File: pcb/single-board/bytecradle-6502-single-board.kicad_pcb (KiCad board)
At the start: 2 copper layers, 224.9 x 116.2 mm, 88 parts, among them J1 USB_B, J2 EXPBUS1, J3 EXPBUS2, J4 VIA, J5 UART1, J6 UART2, J7 Serial, J8 Serial, SW1 SW_SPDT, SW2 RESET, SW3 NMI, U1 74HC14, U10 74HC273, U11 74HC273, U12 74HC245, U13 74HC245, U14 74HC10, U15 SST39SF040, U16 AS6C4008, U17 CY62256, U18 74HC688, U19 W65C22NxP, U2 W65C02, U20 74HC688, U21 W65C51NxP, U22 74HC688, U23 W65C51NxP, U3 74HC688, U4 74HC08, U5 74HC688, U6 74HC688, U7 74HC04, U8 74HC10, U9 74HC00, X1 32MHz, Y1 1.8432 MHz, Y2 1.8432 MHz

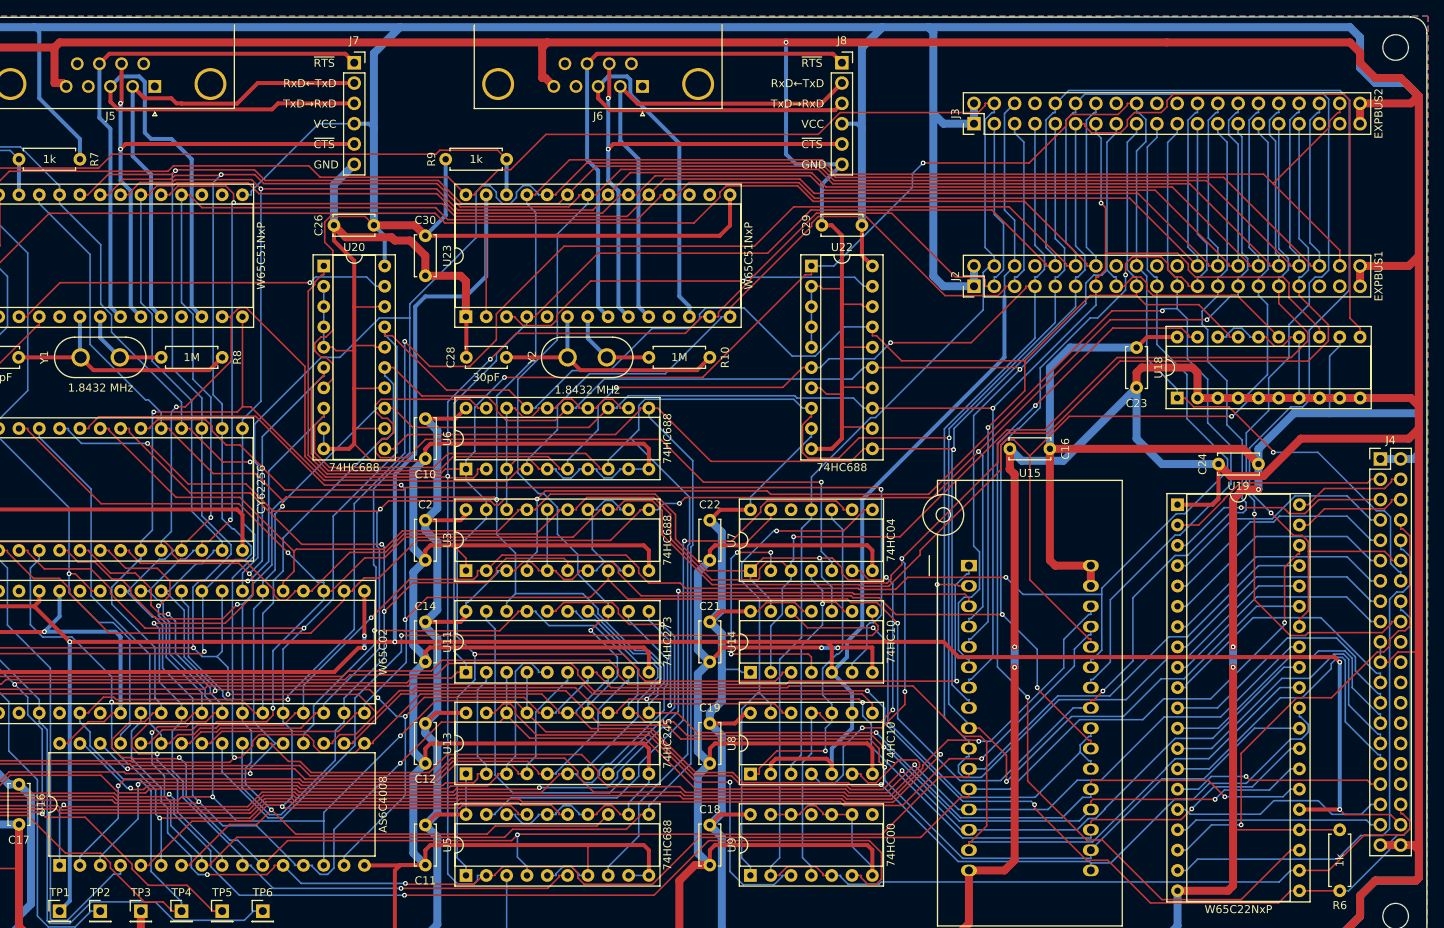
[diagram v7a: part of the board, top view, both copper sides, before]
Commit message: Revising board and adding logo
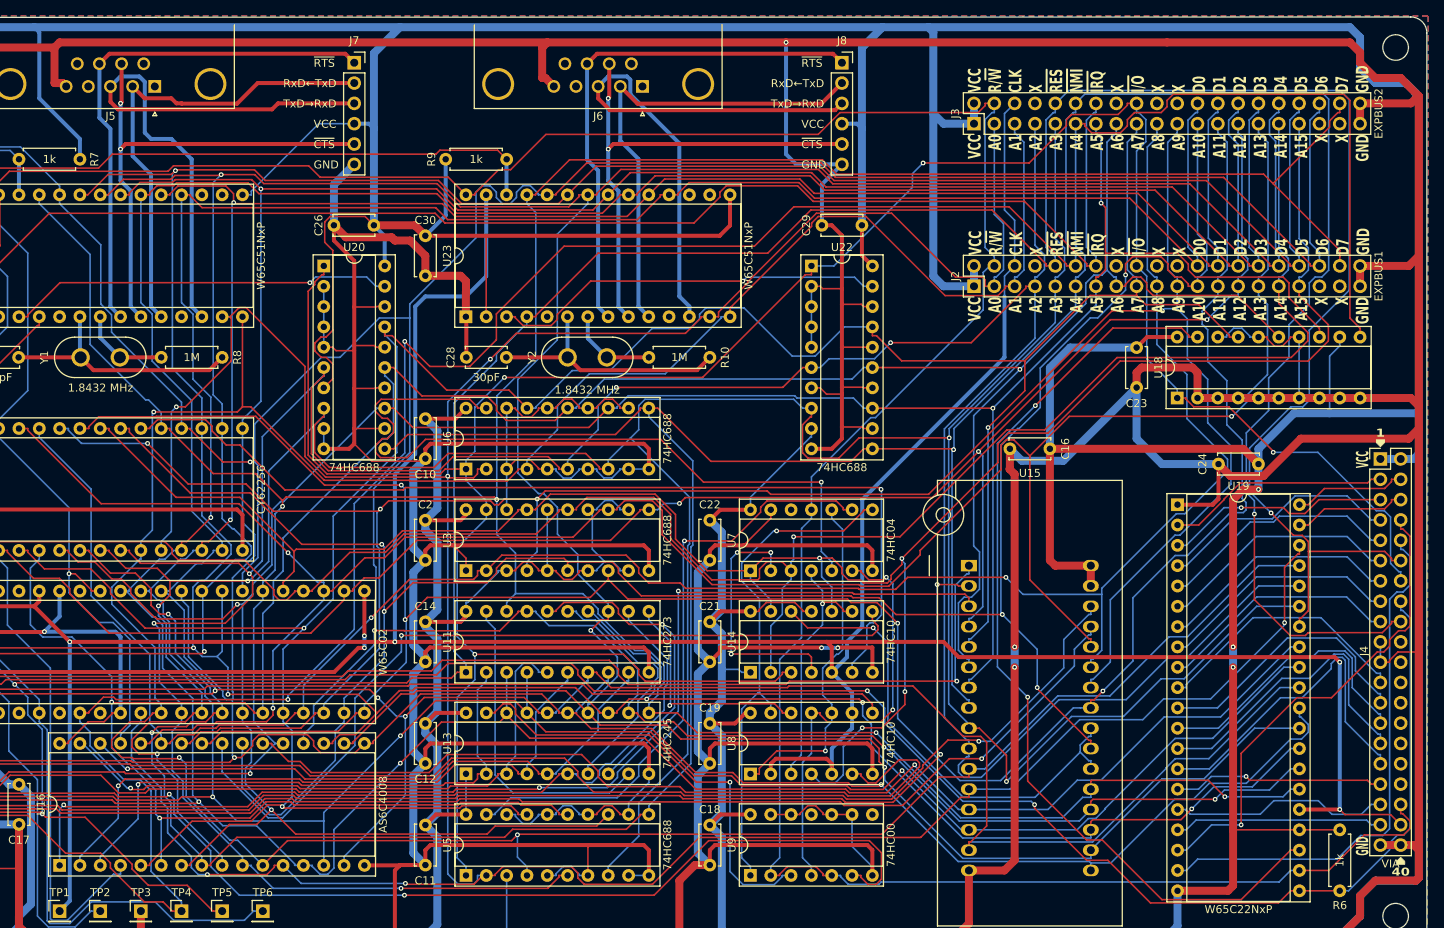
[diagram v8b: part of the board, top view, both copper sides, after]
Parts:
- U16: footprint Package_DIP:DIP-32_W15.24mm -> Package_DIP:DIP-32_W15.24mm_Socket
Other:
- board text added: "1"
- board text added: "40"
- board text added: "VCC A0 A1 A2 A3 A4 A5 A6 A7 A8 A9 A10 A11 A12 A13 A14 A15 X X GND"
- board text added: "VCC R/~{W} CLK X ~{RES} ~{NMI} ~{IRQ} X ~{I/O} X X D0 D1 D2 D3 D4 D5 D6 D7 GND"
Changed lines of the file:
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@@
 		)
 	)
-	(footprint "Package_DIP:DIP-32_W15.24mm"
+	(footprint "Package_DIP:DIP-32_W15.24mm_Socket"
 		(layer "F.Cu")
 		(at 101.6 132.08 90)
-		(descr "32-lead though-hole mounted DIP package, row spacing 15.24 mm (600 mils)")
-		(tags "THT DIP DIL PDIP 2.54mm 15.24mm 600mil")
+		(descr "32-lead though-hole mounted DIP package, row spacing 15.24 mm (600 mils), Socket")
+		(tags "THT DIP DIL PDIP 2.54mm 15.24mm 600mil Socket")
 		(property "Reference" "U16"
-			(at 7.62 -2.33 -90)
+			(at 7.62 -2.33 90)
 			(layer "F.SilkS")
 			(effects
@@
 		)
 		(property "Value" "AS6C4008"
-			(at 7.62 40.43 -90)
+			(at 7.62 40.43 90)
 			(layer "F.SilkS")
 			(effects
@@
 			)
 		)
-		(property "Footprint" "Package_DIP:DIP-32_W15.24mm"
+		(property "Footprint" "Package_DIP:DIP-32_W15.24mm_Socket"
 			(at 0 0 90)
 			(unlocked yes)
@@
 		(attr through_hole)
 		(fp_line
+			(start 16.57 -1.39)
+			(end -1.33 -1.39)
+			(stroke
+				(width 0.12)
+				(type solid)
+			)
+			(layer "F.SilkS")
+		)
+		(fp_line
+			(start -1.33 -1.39)
+			(end -1.33 39.49)
+			(stroke
+				(width 0.12)
+				(type solid)
+			)
+			(layer "F.SilkS")
+		)
+		(fp_line
 			(start 14.08 -1.33)
 			(end 8.62 -1.33)
@@
 			(layer "F.SilkS")
 		)
+		(fp_line
+			(start 16.57 39.49)
+			(end 16.57 -1.39)
+			(stroke
+				(width 0.12)
+				(type solid)
+			)
+			(layer "F.SilkS")
+		)
+		(fp_line
+			(start -1.33 39.49)
+			(end 16.57 39.49)
+			(stroke
+				(width 0.12)
+				(type solid)
+			)
+			(layer "F.SilkS")
+		)
 		(fp_arc
 			(start 8.62 -1.33)
@@
 		)
 		(fp_line
-			(start 16.3 -1.55)
-			(end -1.05 -1.55)
+			(start 16.8 -1.6)
+			(end -1.55 -1.6)
 			(stroke
 				(width 0.05)
@@
 		)
 		(fp_line
-			(start -1.05 -1.55)
-			(end -1.05 39.65)
+			(start -1.55 -1.6)
+			(end -1.55 39.7)
 			(stroke
 				(width 0.05)
@@
 		)
 		(fp_line
-			(start 16.3 39.65)
-			(end 16.3 -1.55)
+			(start 16.8 39.7)
+			(end 16.8 -1.6)
 			(stroke
 				(width 0.05)
@@
 		)
 		(fp_line
-			(start -1.05 39.65)
-			(end 16.3 39.65)
+			(start -1.55 39.7)
+			(end 16.8 39.7)
 			(stroke
 				(width 0.05)
@@
 		)
 		(fp_line
+			(start 16.51 -1.33)
+			(end -1.27 -1.33)
+			(stroke
+				(width 0.1)
+				(type solid)
+			)
+			(layer "F.Fab")
+		)
+		(fp_line
+			(start -1.27 -1.33)
+			(end -1.27 39.43)
+			(stroke
+				(width 0.1)
+				(type solid)
+			)
+			(layer "F.Fab")
+		)
+		(fp_line
 			(start 14.985 -1.27)
 			(end 14.985 39.37)
@@
 			(layer "F.Fab")
 		)
+		(fp_line
+			(start 16.51 39.43)
+			(end 16.51 -1.33)
+			(stroke
+				(width 0.1)
+				(type solid)
+			)
+			(layer "F.Fab")
+		)
+		(fp_line
+			(start -1.27 39.43)
+			(end 16.51 39.43)
+			(stroke
+				(width 0.1)
+				(type solid)
+			)
+			(layer "F.Fab")
+		)
 		(fp_text user "${REFERENCE}"
-			(at 7.62 19.05 -90)
+			(at 7.62 19.05 90)
 			(layer "F.Fab")
 			(effects
@@
 			(pintype "power_in")
 		)
-		(model "${KICAD8_3DMODEL_DIR}/Package_DIP.3dshapes/DIP-32_W15.24mm.wrl"
+		(model "${KICAD8_3DMODEL_DIR}/Package_DIP.3dshapes/DIP-32_W15.24mm_Socket.wrl"
 			(offset
 				(xyz 0 0 0)
@@
 		(tags "Through hole pin header THT 2x20 2.54mm double row")
 		(property "Reference" "J4"
-			(at 1.27 -2.33 0)
+			(at -2.032 24.003 90)
 			(layer "F.SilkS")
 			(effects
@@
 		(property "Value" "VIA"
 			(at 1.27 50.59 0)
-			(layer "F.Fab")
+			(layer "F.SilkS")
 			(effects
 				(font
@@
 		)
 	)
+	(gr_poly
+		(pts
+			(xy 269.748 131.953) (xy 269.748 131.572) (xy 269.24 131.064) (xy 268.732 131.572) (xy 268.732 131.953)
+		)
+		(stroke
+			(width 0.1)
+			(type solid)
+		)
+		(fill solid)
+		(layer "F.SilkS")
+	)
+	(gr_poly
+		(pts
+			(xy 266.192 78.867) (xy 266.192 79.248) (xy 266.7 79.756) (xy 267.208 79.248) (xy 267.208 78.867)
+		)
+		(stroke
+			(width 0.1)
+			(type solid)
+		)
+		(fill solid)
+		(layer "F.SilkS")
+	)
 	(gr_arc
 		(start 47.674214 28.084214)
@@
 		(layer "Edge.Cuts")
 	)
+	(gr_text "VCC\nR/~{W}\nCLK\nX\n~{RES}\n~{NMI}\n~{IRQ}\nX\n~{I/O}\nX\nX\nD0\nD1\nD2\nD3\nD4\nD5\nD6\nD7\nGND"
+		(at 265.4 35.5 90)
+		(layer "F.SilkS" knockout)
+		(effects
+			(font
+				(size 1.585 1)
+				(thickness 0.25)
+				(bold yes)
+			)
+			(justify left bottom)
+		)
+	)
 	(gr_text "VCC"
 		(at 133.35 40.005 0)
@@
 		)
 	)
+	(gr_text "VCC\nA0\nA1\nA2\nA3\nA4\nA5\nA6\nA7\nA8\nA9\nA10\nA11\nA12\nA13\nA14\nA15\nX\nX\nGND"
+		(at 265.4 40.7 90)
+		(layer "F.SilkS" knockout)
+		(effects
+			(font
+				(size 1.585 1)
+				(thickness 0.25)
+				(bold yes)
+			)
+			(justify right bottom)
+		)
+	)
+	(gr_text "VCC\nR/~{W}\nCLK\nX\n~{RES}\n~{NMI}\n~{IRQ}\nX\n~{I/O}\nX\nX\nD0\nD1\nD2\nD3\nD4\nD5\nD6\nD7\nGND"
+		(at 265.49 55.82 90)
+		(layer "F.SilkS" knockout)
+		(effects
+			(font
+				(size 1.585 1)
+				(thickness 0.25)
+				(bold yes)
+			)
+			(justify left bottom)
+		)
+	)
+	(gr_text "VCC\nA0\nA1\nA2\nA3\nA4\nA5\nA6\nA7\nA8\nA9\nA10\nA11\nA12\nA13\nA14\nA15\nX\nX\nGND"
+		(at 265.4 61.02 90)
+		(layer "F.SilkS" knockout)
+		(effects
+			(font
+				(size 1.585 1)
+				(thickness 0.25)
+				(bold yes)
+			)
+			(justify right bottom)
+		)
+	)
 	(gr_text "TxD→RxD"
 		(at 129.54 37.465 0)
@@
 		)
 	)
+	(gr_text "VCC"
+		(at 265.37 82.423 90)
+		(layer "F.SilkS" knockout)
+		(effects
+			(font
+				(size 1.54 0.7)
+				(thickness 0.175)
+				(bold yes)
+			)
+			(justify left bottom)
+		)
+	)
+	(gr_text "GND"
+		(at 265.37 130.87 90)
+		(layer "F.SilkS" knockout)
+		(effects
+			(font
+				(size 1.54 0.7)
+				(thickness 0.175)
+				(bold yes)
+			)
+			(justify left bottom)
+		)
+	)
+	(gr_text "40"
+		(at 269.24 133.477 0)
+		(layer "F.SilkS" knockout)
+		(effects
+			(font
+				(size 1 1.2)
+				(thickness 0.2)
+				(bold yes)
+			)
+			(justify bottom)
+		)
+	)
 	(gr_text "~{RTS}"
 		(at 194.31 32.385 0)
@@
 		)
 	)
+	(gr_text "1"
+		(at 266.7 78.613 0)
+		(layer "F.SilkS" knockout)
+		(effects
+			(font
+				(size 1 1.2)
+				(thickness 0.2)
+				(bold yes)
+			)
+			(justify bottom)
+		)
+	)
